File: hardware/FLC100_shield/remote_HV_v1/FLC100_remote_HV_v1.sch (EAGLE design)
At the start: 25 parts, among them IC1 MCP3424, IC3 LM1702-5V, X1 RJ11-6P6CPTH

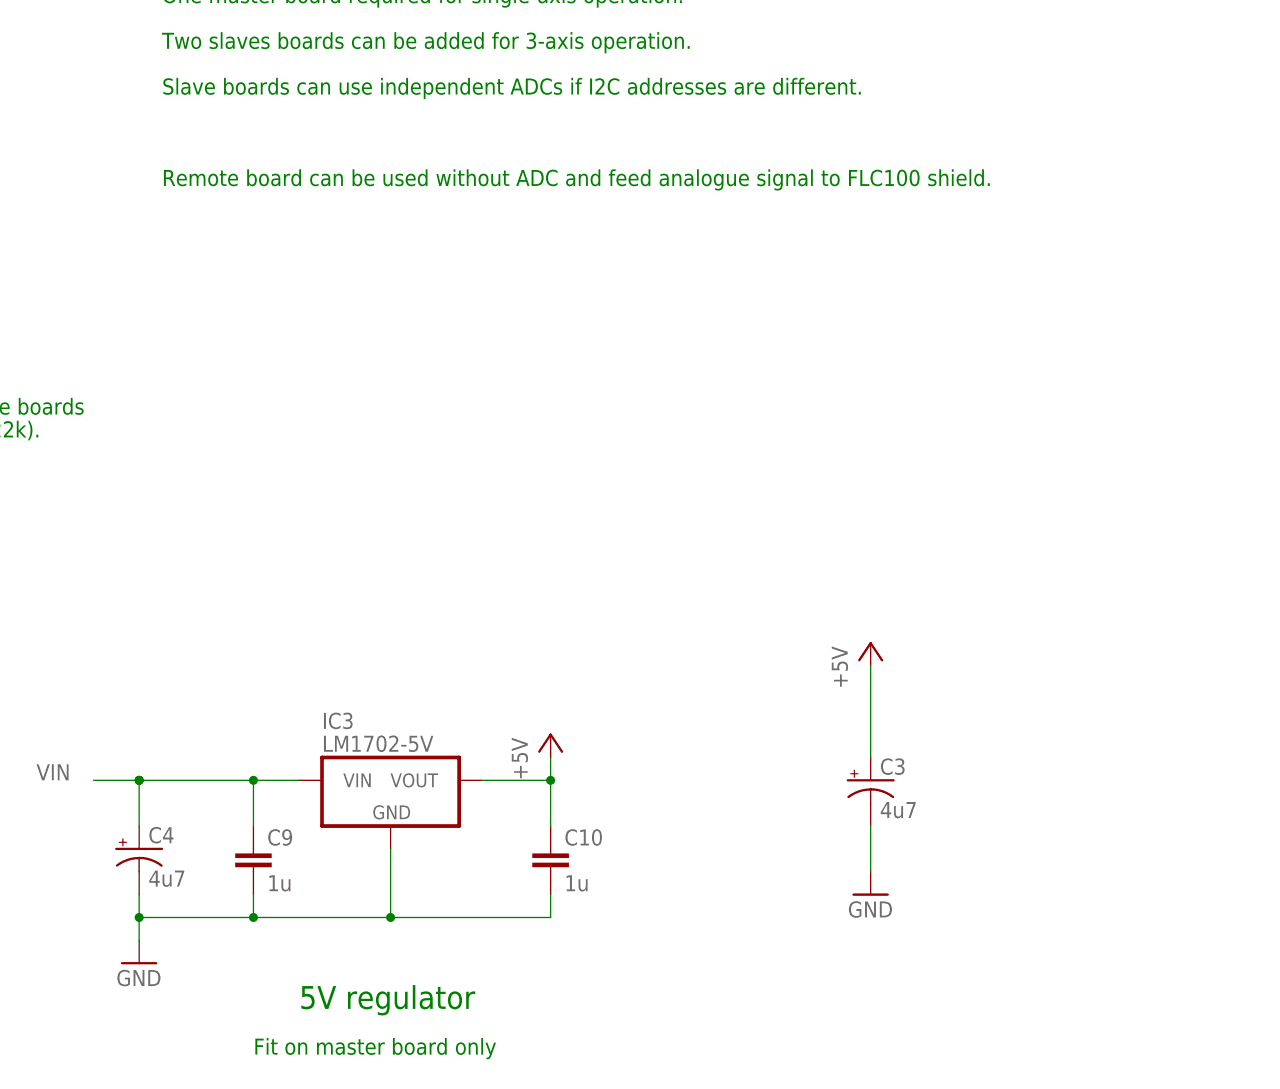
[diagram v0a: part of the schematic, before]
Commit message: Updated MCP3424 footprint for easier hand soldering.
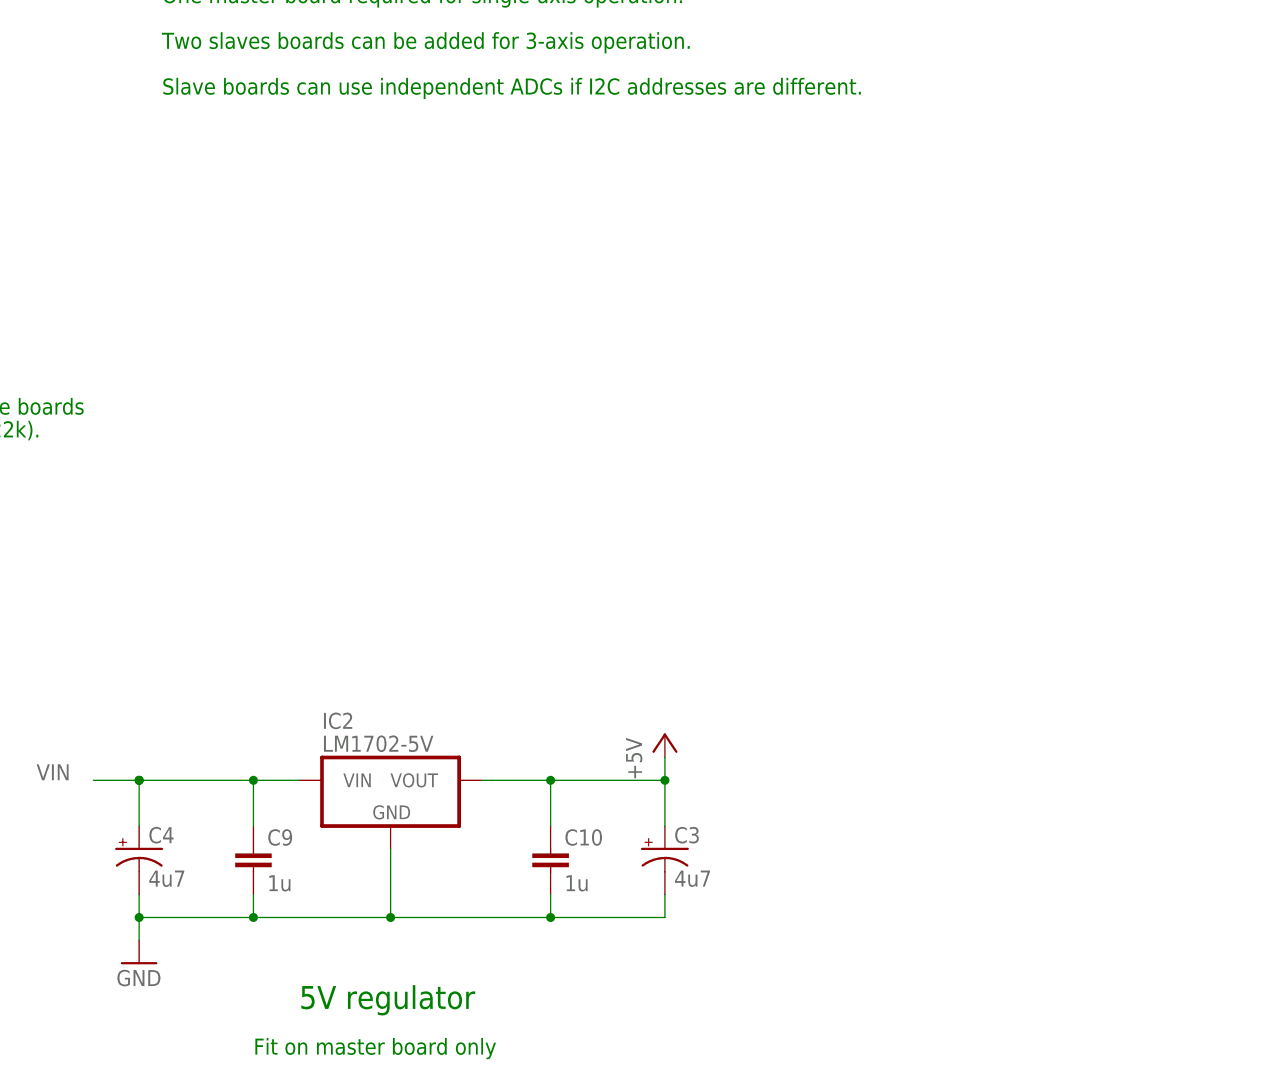
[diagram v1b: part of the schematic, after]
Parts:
- IC1: device SteveMarple:MCP3424-E/SLSO14 -> SteveMarple:MCP3424-E/SLSO14-HAND
- renumbered IC3 to IC2
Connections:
- net N$11 renamed ADDR0
- net N$12 renamed ADDR1
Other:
- note removed: "Remote board can be used without ADC and feed analogue signal to FLC100 shield."
- moved on the sheet: C3
